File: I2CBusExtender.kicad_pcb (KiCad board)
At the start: 2 copper layers, 57.5 x 17.9 mm, 19 parts, among them J1 SBusConn, J2 LBusCon, U1 P82B715

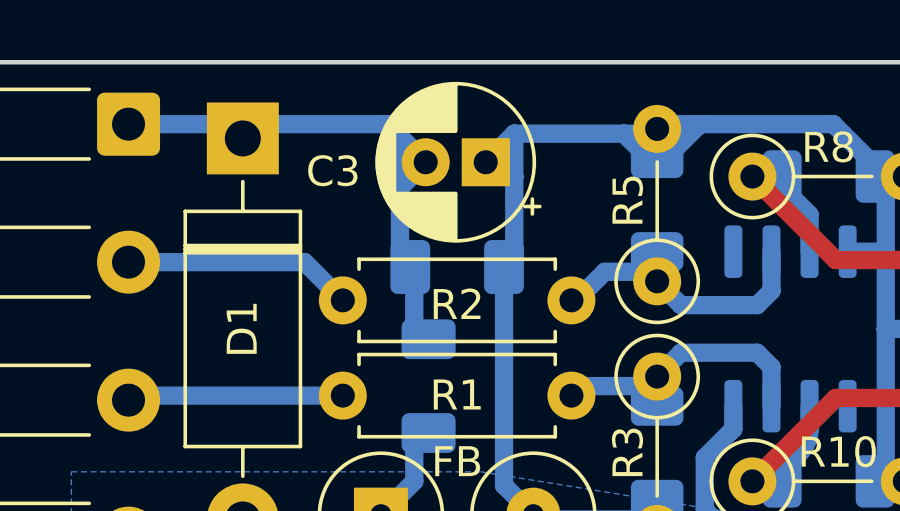
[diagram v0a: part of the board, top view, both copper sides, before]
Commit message: Simplified some tracks.
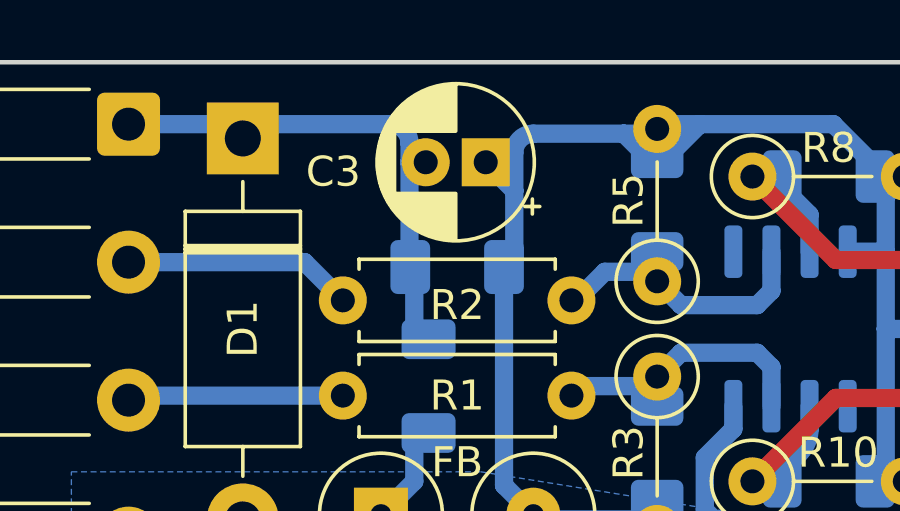
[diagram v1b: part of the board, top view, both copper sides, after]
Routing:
- net /VCC: track 48.2 -> 46.0 mm
- net /Gnd: track 22.0 -> 20.7 mm
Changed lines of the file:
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@@
   (segment (start 91.7575 92.55125) (end 91.7575 94.4325) (width 0.6096) (layer "B.Cu") (net 3))
   (via (at 108.10875 93.18625) (size 1.28) (drill 0.7) (layers "F.Cu" "B.Cu") (net 4))
-  (segment (start 96.99625 79.7875) (end 96.99625 81.5025) (width 0.6096) (layer "B.Cu") (net 4))
+  (segment (start 97.31375 80.01) (end 97.31375 80.645) (width 0.6096) (layer "B.Cu") (net 4))
+  (segment (start 97.31375 80.645) (end 97.31375 84.1125) (width 0.6096) (layer "B.Cu") (net 4))
   (segment (start 108.10875 88.77625) (end 108.10875 89.535) (width 0.6096) (layer "B.Cu") (net 4))
-  (segment (start 92.86875 79.375) (end 96.58375 79.375) (width 0.6096) (layer "B.Cu") (net 4))
+  (segment (start 97.85375 80.645) (end 97.31375 80.645) (width 0.6096) (layer "B.Cu") (net 4))
   (segment (start 108.10875 89.535) (end 107.15625 90.4875) (width 0.6096) (layer "B.Cu") (net 4))
   (segment (start 91.28125 79.375) (end 91.7575 79.85125) (width 0.6096) (layer "B.Cu") (net 4))
-  (segment (start 96.99625 81.5025) (end 96.99625 83.795) (width 0.6096) (layer "B.Cu") (net 4))
+  (segment (start 92.86875 79.375) (end 96.67875 79.375) (width 0.6096) (layer "B.Cu") (net 4))
   (segment (start 107.15625 92.23375) (end 108.10875 93.18625) (width 0.6096) (layer "B.Cu") (net 4))
   (segment (start 107.15625 90.4875) (end 107.15625 92.23375) (width 0.6096) (layer "B.Cu") (net 4))
   (segment (start 87.9475 79.375) (end 91.28125 79.375) (width 0.6096) (layer "B.Cu") (net 4))
-  (segment (start 97.85375 80.645) (end 96.99625 81.5025) (width 0.6096) (layer "B.Cu") (net 4))
-  (segment (start 96.58375 79.375) (end 96.99625 79.7875) (width 0.6096) (layer "B.Cu") (net 4))
-  (segment (start 96.99625 79.7875) (end 97.85375 80.645) (width 0.6096) (layer "B.Cu") (net 4))
   (segment (start 97.4725 86.54375) (end 97.4725 84.455) (width 0.6096) (layer "B.Cu") (net 4))
+  (arc (start 96.67875 79.375) (mid 97.127763 79.560987) (end 97.31375 80.01) (width 0.6096) (layer "B.Cu") (net 4))
   (segment (start 93.8175 83.975) (end 95.09125 85.24875) (width 0.6096) (layer "B.Cu") (net 5))
   (segment (start 87.9475 83.975) (end 93.8175 83.975) (width 0.6096) (layer "B.Cu") (net 5))
@@
   (segment (start 110.64875 82.39125) (end 109.69625 81.43875) (width 0.6096) (layer "B.Cu") (net 8))
   (segment (start 110.64875 83.62625) (end 110.64875 82.39125) (width 0.6096) (layer "B.Cu") (net 8))
+  (segment (start 100.80625 80.3275) (end 100.80625 81.5975) (width 0.6096) (layer "B.Cu") (net 9))
   (segment (start 114.48375 86.20125) (end 113.18875 86.20125) (width 0.6096) (layer "B.Cu") (net 9))
   (segment (start 101.6 92.55125) (end 101.44125 92.3925) (width 0.6096) (layer "B.Cu") (net 9))
@@
   (segment (start 105.7275 79.375) (end 106.9975 79.375) (width 0.6096) (layer "B.Cu") (net 9))
   (segment (start 105.25125 92.55125) (end 101.6 92.55125) (width 0.6096) (layer "B.Cu") (net 9))
-  (segment (start 100.80625 79.6925) (end 100.80625 81.12125) (width 0.6096) (layer "B.Cu") (net 9))
   (segment (start 113.18875 83.62625) (end 113.18875 81.75625) (width 0.6096) (layer "B.Cu") (net 9))
   (segment (start 100.46375 84.1375) (end 100.46375 91.415) (width 0.6096) (layer "B.Cu") (net 9))
-  (segment (start 100.80625 81.12125) (end 99.3775 81.12125) (width 0.6096) (layer "B.Cu") (net 9))
   (segment (start 104.4575 79.6925) (end 105.56875 79.6925) (width 0.6096) (layer "B.Cu") (net 9))
+  (segment (start 104.4575 79.6925) (end 101.44125 79.6925) (width 0.6096) (layer "B.Cu") (net 9))
   (segment (start 100.46375 91.415) (end 101.44125 92.3925) (width 0.6096) (layer "B.Cu") (net 9))
   (segment (start 113.18875 81.75625) (end 113.82375 81.12125) (width 0.6096) (layer "B.Cu") (net 9))
-  (segment (start 104.4575 79.6925) (end 100.80625 79.6925) (width 0.6096) (layer "B.Cu") (net 9))
   (segment (start 111.4425 79.375) (end 112.55375 80.48625) (width 0.6096) (layer "B.Cu") (net 9))
-  (segment (start 100.80625 83.795) (end 100.46375 84.1375) (width 0.6096) (layer "B.Cu") (net 9))
-  (segment (start 100.80625 79.6925) (end 99.85375 80.645) (width 0.6096) (layer "B.Cu") (net 9))
+  (segment (start 99.85375 80.645) (end 100.80625 81.5975) (width 0.6096) (layer "B.Cu") (net 9))
+  (segment (start 100.80625 81.5975) (end 100.80625 83.795) (width 0.6096) (layer "B.Cu") (net 9))
   (segment (start 113.18875 83.62625) (end 111.91875 83.62625) (width 0.6096) (layer "B.Cu") (net 9))
   (segment (start 113.18875 91.00125) (end 113.18875 86.20125) (width 0.6096) (layer "B.Cu") (net 9))
-  (segment (start 100.80625 81.12125) (end 100.80625 83.795) (width 0.6096) (layer "B.Cu") (net 9))
+  (arc (start 101.44125 79.6925) (mid 100.992237 79.878487) (end 100.80625 80.3275) (width 0.6096) (layer "B.Cu") (net 9))
   (zone (net 4) (net_name "/Gnd") (layers F&B.Cu) (name "GroundPlanes") (hatch edge 0.508)
     (connect_pads (clearance 0.508))
